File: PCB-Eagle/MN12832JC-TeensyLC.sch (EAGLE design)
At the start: 46 parts, among them IC4 ZXBM5210, IC6 74HC132D, SW3 EC12E_SW, SW4 EC12E_SW

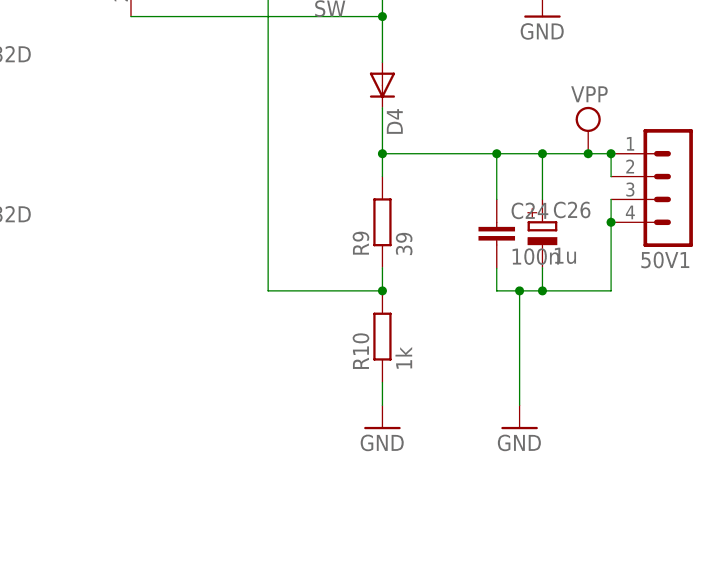
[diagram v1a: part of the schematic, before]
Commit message: fixed Up Converter R9/R10 twist, adjusted values for 50V
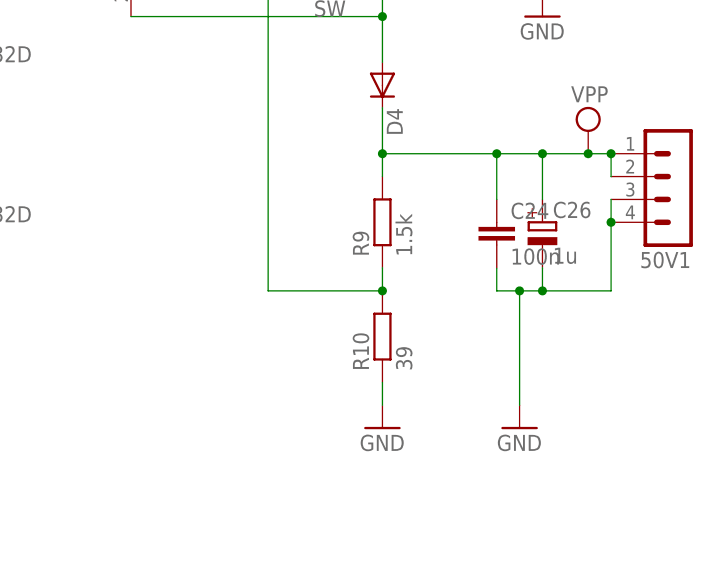
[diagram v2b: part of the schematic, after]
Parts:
- R10: value 1k -> 39
- R9: value 39 -> 1.5k
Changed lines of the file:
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@@
 <?xml version="1.0" encoding="utf-8"?>
 <!DOCTYPE eagle SYSTEM "eagle.dtd">
-<eagle version="9.5.2">
+<eagle version="9.5.1">
 <drawing>
 <settings>
@@
 <part name="P+11" library="supply1" library_urn="urn:adsk.eagle:library:371" deviceset="+5V" device=""/>
 <part name="D4" library="diode" library_urn="urn:adsk.eagle:library:210" deviceset="DIODE-" device="SMB" package3d_urn="urn:adsk.eagle:package:43404/2"/>
-<part name="R9" library="rcl" library_urn="urn:adsk.eagle:library:334" deviceset="R-EU_" device="R1206" package3d_urn="urn:adsk.eagle:package:23540/2" value="39"/>
-<part name="R10" library="rcl" library_urn="urn:adsk.eagle:library:334" deviceset="R-EU_" device="R1206" package3d_urn="urn:adsk.eagle:package:23540/2" value="1k"/>
+<part name="R9" library="rcl" library_urn="urn:adsk.eagle:library:334" deviceset="R-EU_" device="R1206" package3d_urn="urn:adsk.eagle:package:23540/2" value="1.5k"/>
+<part name="R10" library="rcl" library_urn="urn:adsk.eagle:library:334" deviceset="R-EU_" device="R1206" package3d_urn="urn:adsk.eagle:package:23540/2" value="39"/>
 <part name="GND27" library="supply1" library_urn="urn:adsk.eagle:library:371" deviceset="GND" device=""/>
 <part name="C24" library="rcl" library_urn="urn:adsk.eagle:library:334" deviceset="C-EU" device="C1206" package3d_urn="urn:adsk.eagle:package:23618/2" value="100n"/>

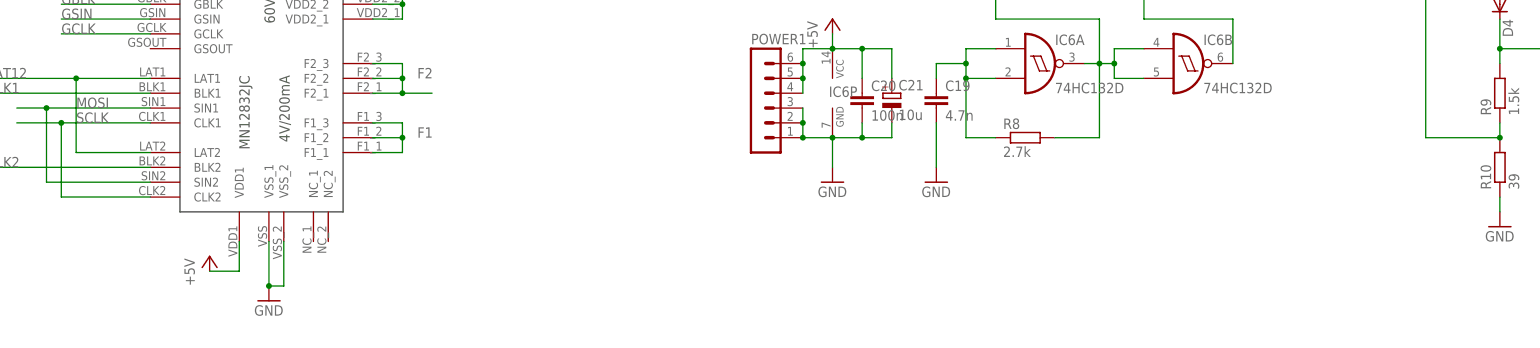
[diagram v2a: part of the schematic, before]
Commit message: Added Voltage drop diode for Vdd1, lowered Fillament frequency to avoid off time
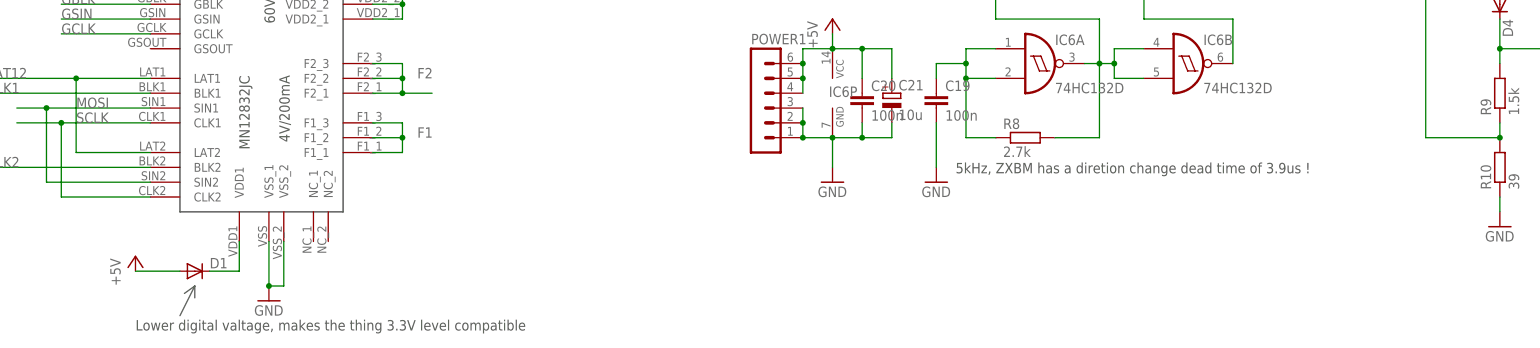
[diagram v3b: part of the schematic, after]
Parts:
- added D1: (no value), diode:DIODE-SMB
- C19: value 4.7n -> 100n
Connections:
- new net N$3: D1.C, U$1.VDD1
- net +5V: now also D1.A; no longer U$1.VDD1
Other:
- note added: "5kHz, ZXBM has a diretion change dead time of 3.9us !"
- note added: "Lower digital valtage, makes the thing 3.3V level compatible"
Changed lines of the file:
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@@
 <layer number="97" name="Info" color="7" fill="1" visible="yes" active="yes"/>
 <layer number="98" name="Guide" color="6" fill="1" visible="yes" active="yes"/>
-<layer number="99" name="SpiceOrder" color="5" fill="1" visible="yes" active="yes"/>
+<layer number="99" name="SpiceOrder" color="5" fill="1" visible="no" active="yes"/>
 </layers>
 <schematic xreflabel="%F%N/%S.%C%R" xrefpart="/%S.%C%R">
@@
 <part name="SW4" library="vfds" deviceset="EC12E_SW" device="" package3d_urn="urn:adsk.eagle:package:27083/1"/>
 <part name="R8" library="rcl" library_urn="urn:adsk.eagle:library:334" deviceset="R-EU_" device="R1206" package3d_urn="urn:adsk.eagle:package:23540/2" value="2.7k"/>
-<part name="C19" library="rcl" library_urn="urn:adsk.eagle:library:334" deviceset="C-EU" device="C1206" package3d_urn="urn:adsk.eagle:package:23618/2" value="4.7n"/>
+<part name="C19" library="rcl" library_urn="urn:adsk.eagle:library:334" deviceset="C-EU" device="C1206" package3d_urn="urn:adsk.eagle:package:23618/2" value="100n"/>
 <part name="GND21" library="supply1" library_urn="urn:adsk.eagle:library:371" deviceset="GND" device=""/>
 <part name="IC4" library="vfds" deviceset="ZXBM5210" device=""/>
@@
 <part name="R12" library="rcl" library_urn="urn:adsk.eagle:library:334" deviceset="R-EU_" device="0411/15" package3d_urn="urn:adsk.eagle:package:23568/1" value="22"/>
 <part name="L1" library="rcl" library_urn="urn:adsk.eagle:library:334" deviceset="L-EU" device="L1812" package3d_urn="urn:adsk.eagle:package:23494/2" value="10u"/>
+<part name="D1" library="diode" library_urn="urn:adsk.eagle:library:210" deviceset="DIODE-" device="SMB" package3d_urn="urn:adsk.eagle:package:43404/2"/>
 </parts>
 <sheets>
 <sheet>
 <plain>
+<text x="287.782" y="19.304" size="1.778" layer="97">5kHz, ZXBM has a diretion change dead time of 3.9us !</text>
+<text x="147.32" y="-7.62" size="1.778" layer="97">Lower digital valtage, makes the thing 3.3V level compatible</text>
+<wire x1="154.94" y1="-5.08" x2="157.48" y2="0" width="0.1524" layer="97"/>
+<wire x1="157.48" y1="-2.032" x2="157.48" y2="0" width="0.1524" layer="97"/>
+<wire x1="157.48" y1="0" x2="155.702" y2="-1.27" width="0.1524" layer="97"/>
 </plain>
 <instances>
@@
 <attribute name="VALUE" x="191.135" y="61.595" size="1.778" layer="96"/>
 </instance>
-<instance part="P+2" gate="1" x="160.02" y="5.08" smashed="yes">
-<attribute name="VALUE" x="157.48" y="0" size="1.778" layer="96" rot="R90"/>
+<instance part="P+2" gate="1" x="147.32" y="5.08" smashed="yes">
+<attribute name="VALUE" x="144.78" y="0" size="1.778" layer="96" rot="R90"/>
 </instance>
 <instance part="U$3" gate="G$1" x="91.44" y="38.1" smashed="yes">
@@
 <attribute name="NAME" x="285.75" y="79.7814" size="1.778" layer="95" rot="R180"/>
 <attribute name="VALUE" x="285.75" y="84.582" size="1.778" layer="96" rot="R180"/>
+</instance>
+<instance part="D1" gate="G$1" x="157.48" y="2.54" smashed="yes">
+<attribute name="NAME" x="160.02" y="3.0226" size="1.778" layer="95"/>
+<attribute name="VALUE" x="160.02" y="0.2286" size="1.778" layer="96"/>
 </instance>
 </instances>
@@
 <wire x1="129.54" y1="66.04" x2="129.54" y2="78.74" width="0.1524" layer="91"/>
 <pinref part="U$3" gate="G$1" pin="VIN"/>
-</segment>
-<segment>
-<pinref part="P+2" gate="1" pin="+5V"/>
-<wire x1="160.02" y1="2.54" x2="165.1" y2="2.54" width="0.1524" layer="91"/>
-<wire x1="165.1" y1="2.54" x2="165.1" y2="7.62" width="0.1524" layer="91"/>
-<pinref part="U$1" gate="G$1" pin="VDD1"/>
 </segment>
 <segment>
@@
 <pinref part="P+12" gate="1" pin="+5V"/>
 <wire x1="276.86" y1="66.04" x2="276.86" y2="68.58" width="0.1524" layer="91"/>
+</segment>
+<segment>
+<pinref part="D1" gate="G$1" pin="A"/>
+<pinref part="P+2" gate="1" pin="+5V"/>
+<wire x1="154.94" y1="2.54" x2="147.32" y2="2.54" width="0.1524" layer="91"/>
 </segment>
 </net>
@@
 </segment>
 </net>
+<net name="N$3" class="1">
+<segment>
+<wire x1="165.1" y1="2.54" x2="165.1" y2="7.62" width="0.1524" layer="91"/>
+<pinref part="U$1" gate="G$1" pin="VDD1"/>
+<pinref part="D1" gate="G$1" pin="C"/>
+<wire x1="165.1" y1="2.54" x2="160.02" y2="2.54" width="0.1524" layer="91"/>
+</segment>
+</net>

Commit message: minor stuff
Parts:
- R11, R8: value 2.7k -> 4.7k
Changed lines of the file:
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@@
 <part name="SW3" library="vfds" deviceset="EC12E_SW" device="" package3d_urn="urn:adsk.eagle:package:27083/1"/>
 <part name="SW4" library="vfds" deviceset="EC12E_SW" device="" package3d_urn="urn:adsk.eagle:package:27083/1"/>
-<part name="R8" library="rcl" library_urn="urn:adsk.eagle:library:334" deviceset="R-EU_" device="R1206" package3d_urn="urn:adsk.eagle:package:23540/2" value="2.7k"/>
+<part name="R8" library="rcl" library_urn="urn:adsk.eagle:library:334" deviceset="R-EU_" device="R1206" package3d_urn="urn:adsk.eagle:package:23540/2" value="4.7k"/>
 <part name="C19" library="rcl" library_urn="urn:adsk.eagle:library:334" deviceset="C-EU" device="C1206" package3d_urn="urn:adsk.eagle:package:23618/2" value="100n"/>
 <part name="GND21" library="supply1" library_urn="urn:adsk.eagle:library:371" deviceset="GND" device=""/>
@@
 <part name="50V1" library="con-lstb" library_urn="urn:adsk.eagle:library:162" deviceset="MA04-1" device="" package3d_urn="urn:adsk.eagle:package:8337/1"/>
 <part name="IC6" library="74xx-eu" library_urn="urn:adsk.eagle:library:85" deviceset="74*132" device="D" package3d_urn="urn:adsk.eagle:package:2007/1" technology="HC"/>
-<part name="R11" library="rcl" library_urn="urn:adsk.eagle:library:334" deviceset="R-EU_" device="R1206" package3d_urn="urn:adsk.eagle:package:23540/2" value="2.7k"/>
+<part name="R11" library="rcl" library_urn="urn:adsk.eagle:library:334" deviceset="R-EU_" device="R1206" package3d_urn="urn:adsk.eagle:package:23540/2" value="4.7k"/>
 <part name="P+12" library="supply1" library_urn="urn:adsk.eagle:library:371" deviceset="+5V" device=""/>
 <part name="R12" library="rcl" library_urn="urn:adsk.eagle:library:334" deviceset="R-EU_" device="0411/15" package3d_urn="urn:adsk.eagle:package:23568/1" value="22"/>

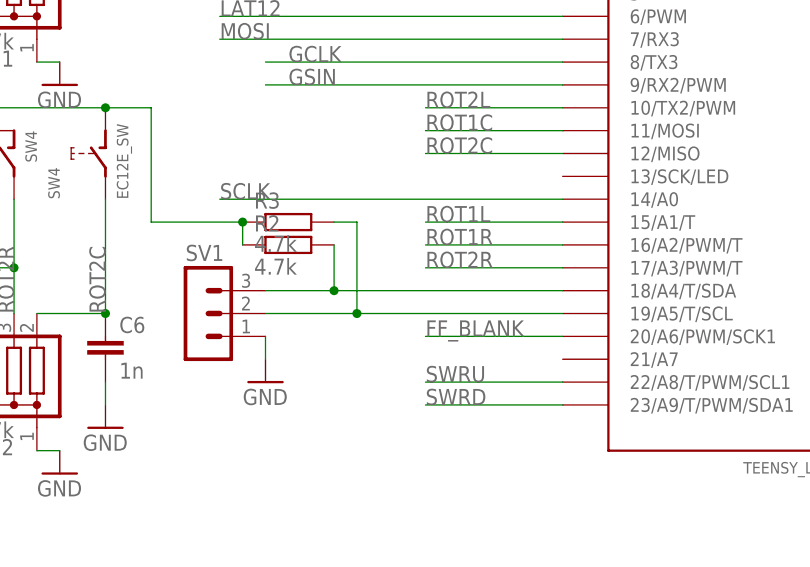
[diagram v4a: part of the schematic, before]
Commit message: added FreeDSP controller. Reads Levels. Sets Volume.
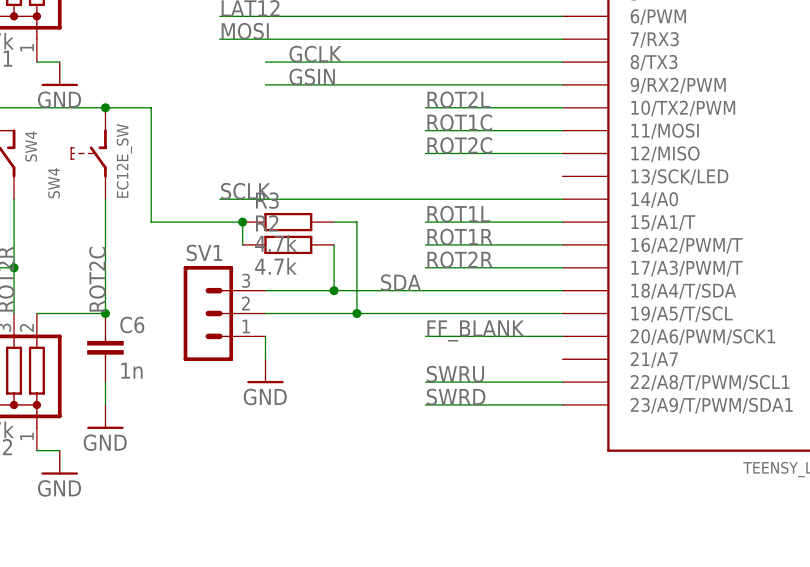
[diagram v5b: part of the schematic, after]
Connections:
- net N$1 renamed SCL
- net N$2 renamed SDA
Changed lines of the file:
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@@
 </segment>
 </net>
-<net name="N$1" class="0">
+<net name="SCL" class="0">
 <segment>
 <pinref part="SV1" gate="G$1" pin="2"/>
@@
 </segment>
 </net>
-<net name="N$2" class="0">
+<net name="SDA" class="0">
 <segment>
 <pinref part="SV1" gate="G$1" pin="3"/>
@@
 <wire x1="43.18" y1="27.94" x2="43.18" y2="22.86" width="0.1524" layer="91"/>
 <junction x="43.18" y="22.86"/>
+<label x="48.26" y="22.86" size="1.778" layer="95"/>
 </segment>
 </net>
